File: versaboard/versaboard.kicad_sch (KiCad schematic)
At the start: 23 parts, among them J1 UART, J39 Conn_02x20_Odd_Even, J4 DBG, J40 Conn_02x20_Odd_Even, SW1 RST, U1 ATSAML21G18B-AUT, Y1 32.768kHz

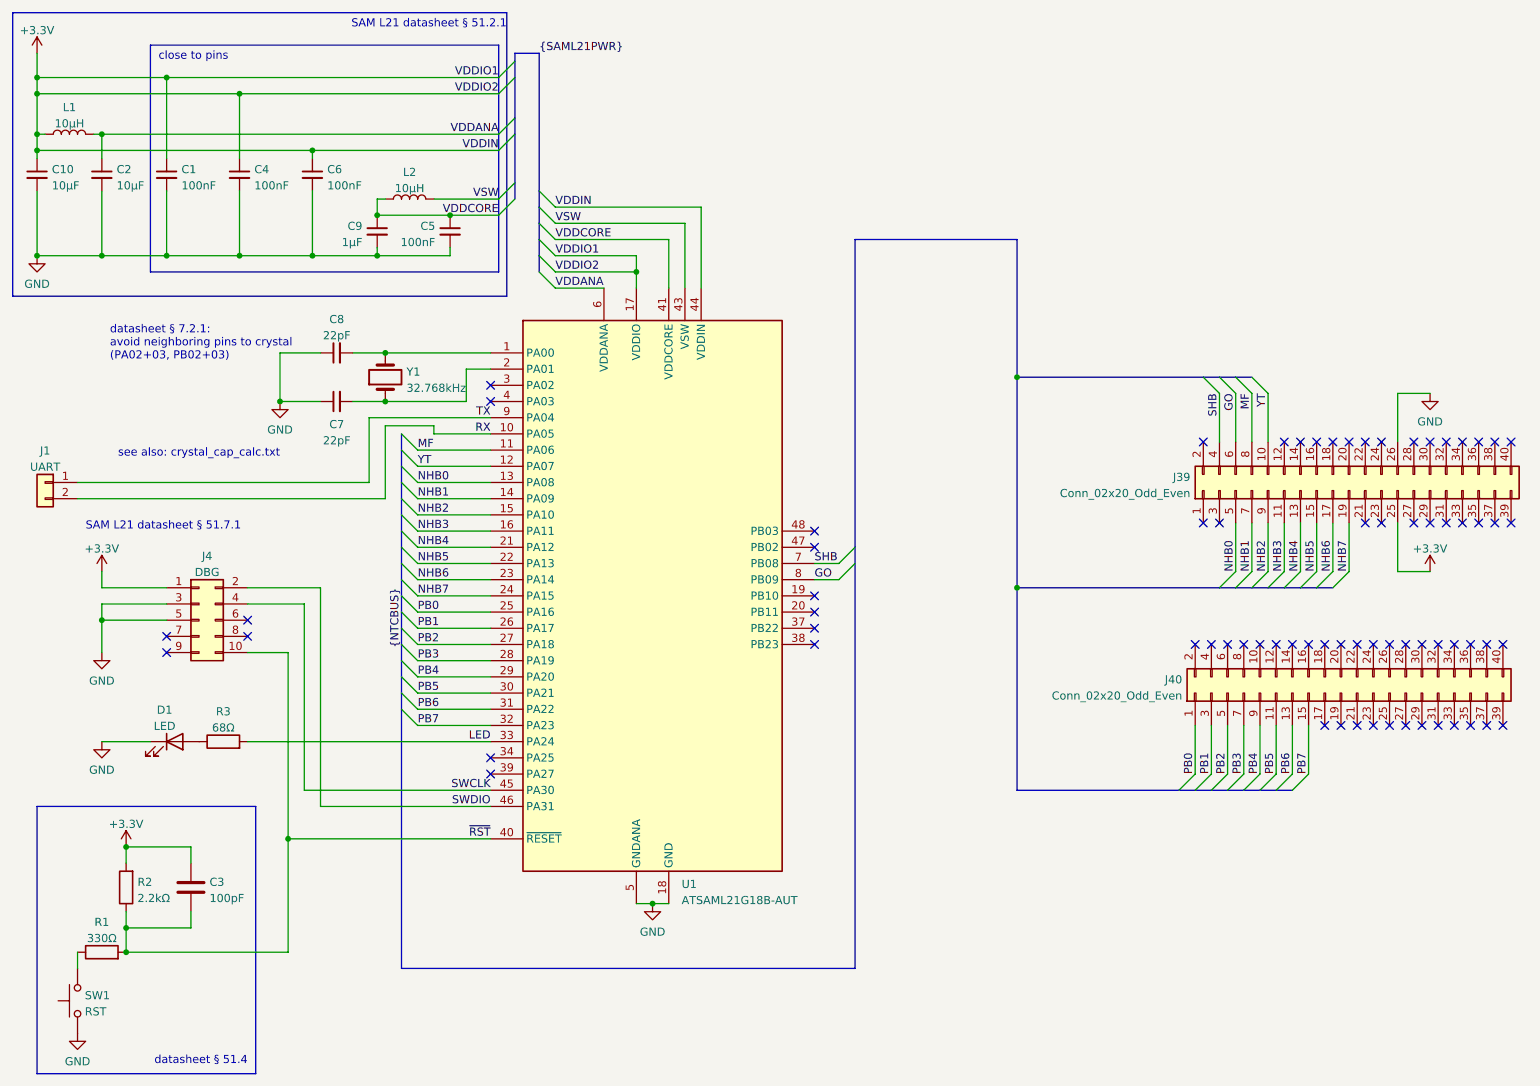
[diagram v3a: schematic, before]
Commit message: versaboard r0002: replace crystal with oscillator, add test points
the crystal on the test run of r0001 does not stabilize; switch to an
oscillator which should manage this without our support

also add a few test points on the board
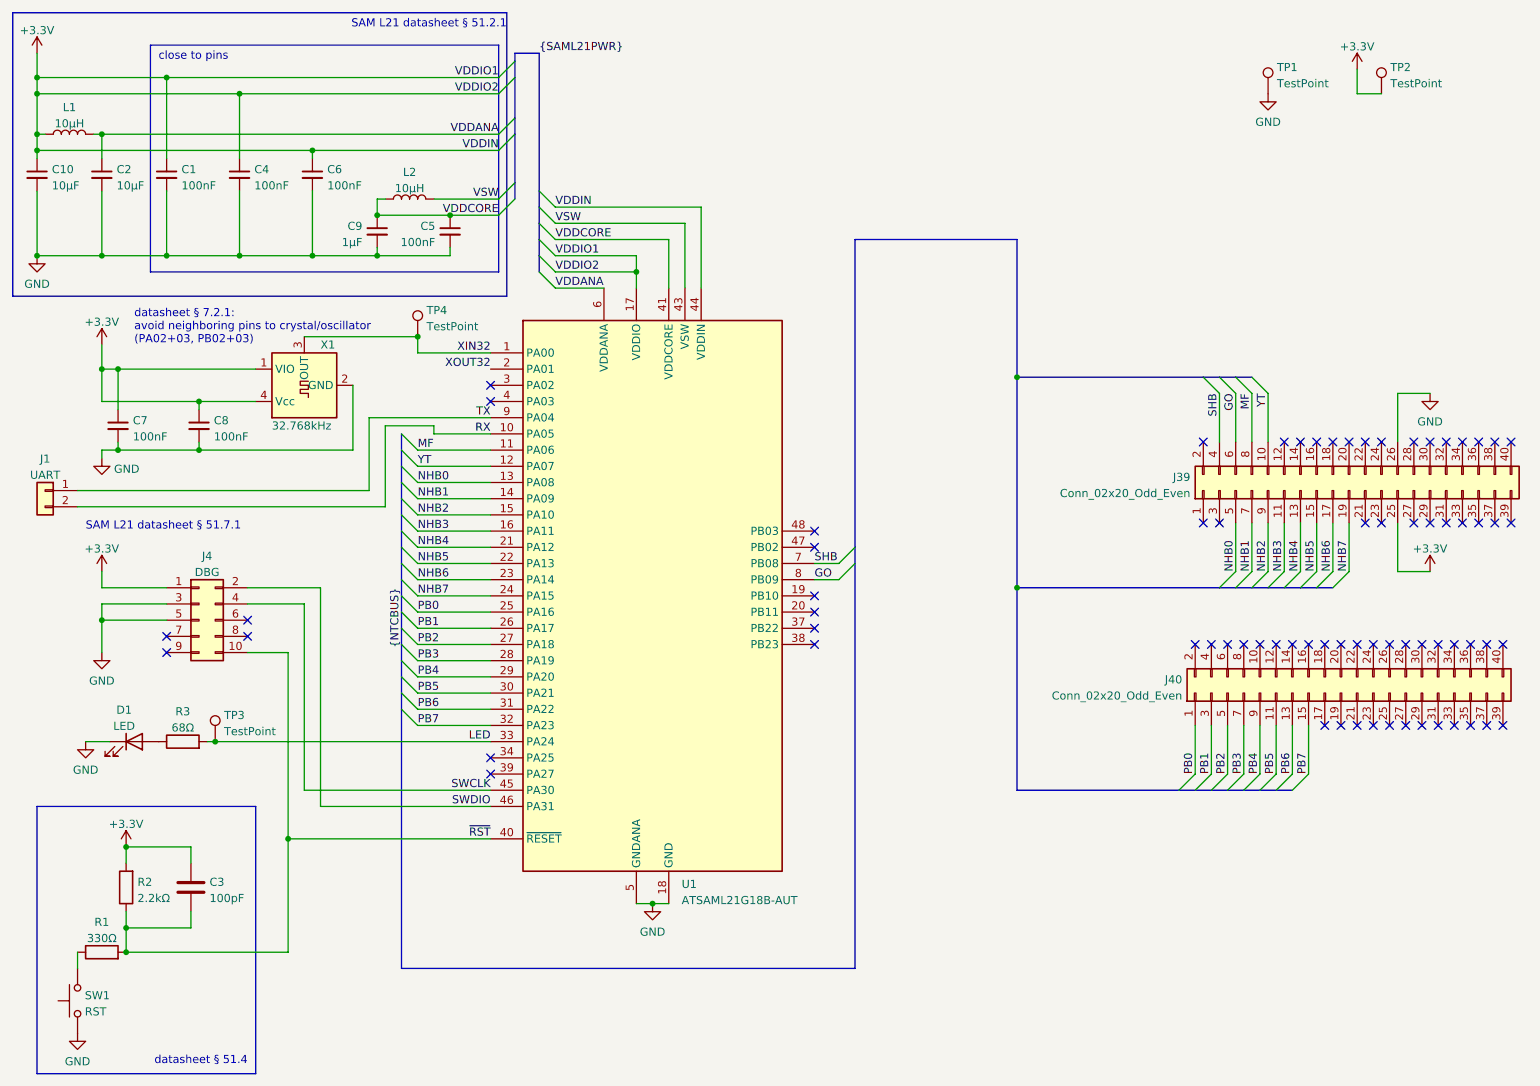
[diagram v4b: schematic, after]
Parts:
- added TP1, TP2, TP3, TP4: TestPoint, TestPoint:TestPoint_Pad_D1.0mm, symbol Connector:TestPoint
- C7, C8: value 22pF -> 100nF; JLCPCB C1555 -> C307331; LCSC C1555 -> C307331
- X1: renamed from Y1; footprint Crystal:Crystal_SMD_3215-2Pin_3.2x1.5mm -> Oscillator:Oscillator_SMD_SeikoEpson_SG3030CM; symbol Device:Crystal -> Oscillator:SG-3030CM; JLCPCB C32346 -> C2976104; LCSC C32346 -> C2976104; Manufacturer (none) -> Seiko Epson; Model (none) -> SG-3031CM
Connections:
- net +3.3V: now also C7.1, C8.1, X1.1 (VIO), X1.4 (Vcc), TP2.1
- net GND: now also C7.2, C8.2, X1.2 (GND), TP1.1; no longer C7.1, C8.1
- net LED: now also TP3.1
- new net XIN32: TP4.1, U1.1 (PA00), X1.3 (OUT)
- new net XOUT32: U1.2 (PA01)
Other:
- note added: "datasheet § 7.2.1: avoid neighboring pins to crystal/oscillator (PA02+03, PB02+03)"
- note removed: "datasheet § 7.2.1: avoid neighboring pins to crystal (PA02+03, PB02+03)"
- note removed: "see also: crystal_cap_calc.txt"
- moved on the sheet: D1, J1, R3

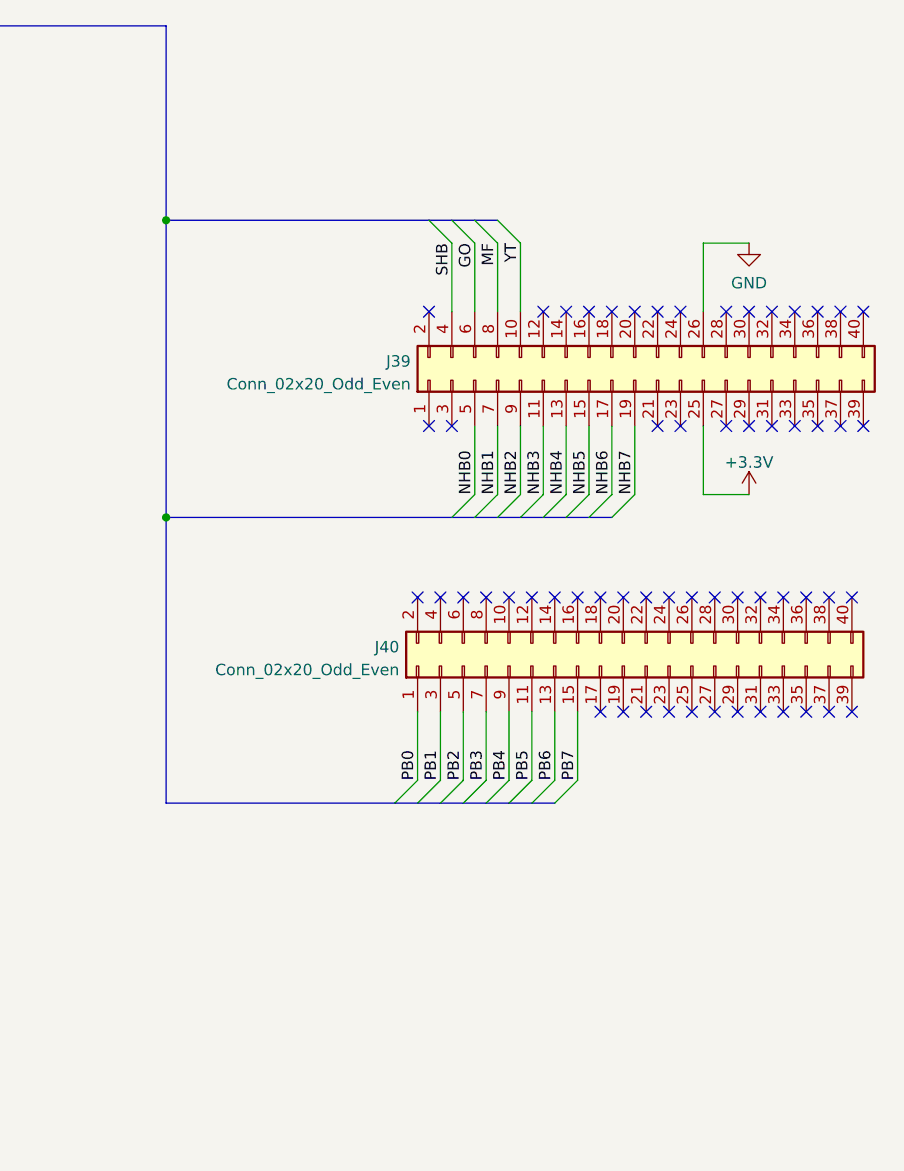
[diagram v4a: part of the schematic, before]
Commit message: versaboard r0003: avoid FPGA pin bank 1
Pin bank 1 on the ECP5 evaluation board is +2.5V by default and this can
only be changed by resoldering SMD resistors. Yeah, no.
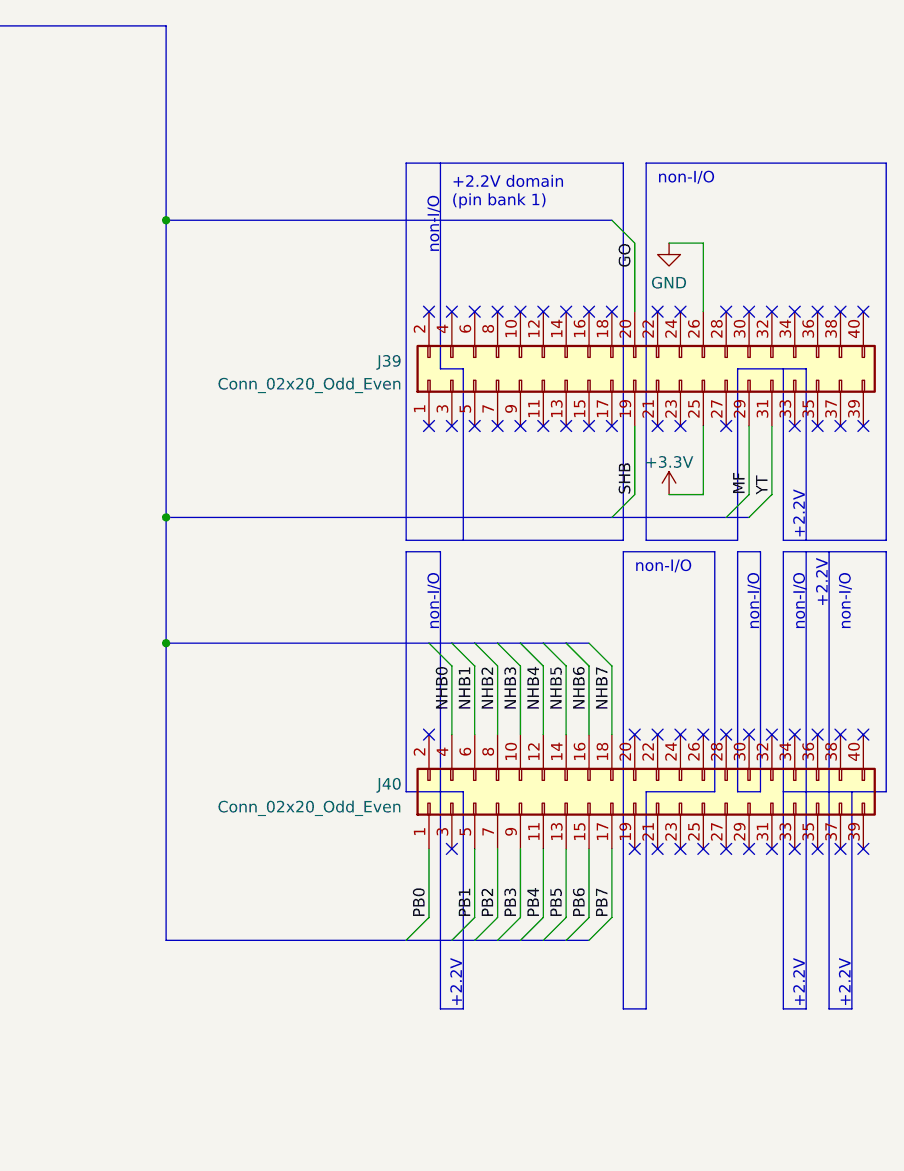
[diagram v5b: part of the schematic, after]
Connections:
- net GO: now also J39.20 (Pin_20); no longer J39.6 (Pin_6)
- net MF: now also J39.29 (Pin_29); no longer J39.8 (Pin_8)
- net NHB0: now also J40.4 (Pin_4); no longer J39.5 (Pin_5)
- net NHB1: now also J40.6 (Pin_6); no longer J39.7 (Pin_7)
- net NHB2: now also J40.8 (Pin_8); no longer J39.9 (Pin_9)
- net NHB3: now also J40.10 (Pin_10); no longer J39.11 (Pin_11)
- net NHB4: now also J40.12 (Pin_12); no longer J39.13 (Pin_13)
- net NHB5: now also J40.14 (Pin_14); no longer J39.15 (Pin_15)
- net NHB6: now also J40.16 (Pin_16); no longer J39.17 (Pin_17)
- net NHB7: now also J40.18 (Pin_18); no longer J39.19 (Pin_19)
- net PB1: now also J40.5 (Pin_5); no longer J40.3 (Pin_3)
- net PB2: now also J40.7 (Pin_7); no longer J40.5 (Pin_5)
- net PB3: now also J40.9 (Pin_9); no longer J40.7 (Pin_7)
- net PB4: now also J40.11 (Pin_11); no longer J40.9 (Pin_9)
- net PB5: now also J40.13 (Pin_13); no longer J40.11 (Pin_11)
- net PB6: now also J40.15 (Pin_15); no longer J40.13 (Pin_13)
- net PB7: now also J40.17 (Pin_17); no longer J40.15 (Pin_15)
- net SHB: now also J39.19 (Pin_19); no longer J39.4 (Pin_4)
- net YT: now also J39.31 (Pin_31); no longer J39.10 (Pin_10)
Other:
- note added: "+2.2V"
- note added: "+2.2V domain (pin bank 1)"
- note added: "non-I/O"
- moved on the sheet: J40

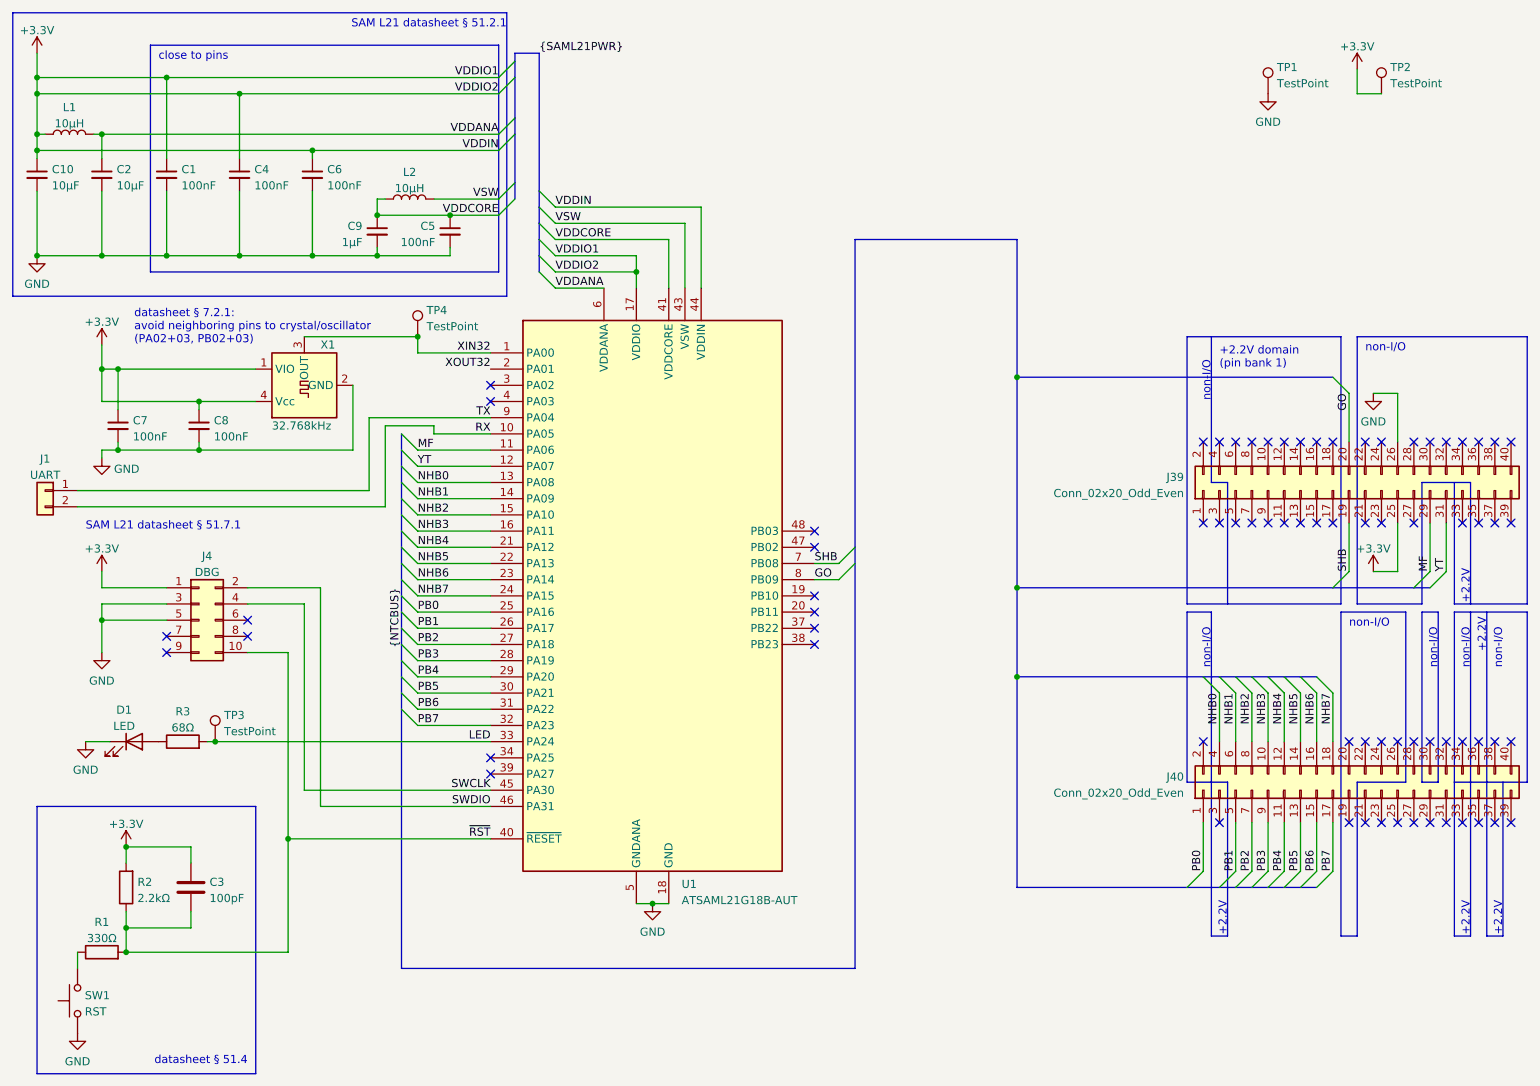
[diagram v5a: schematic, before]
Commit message: versaboard: add STA, STC and SG pins
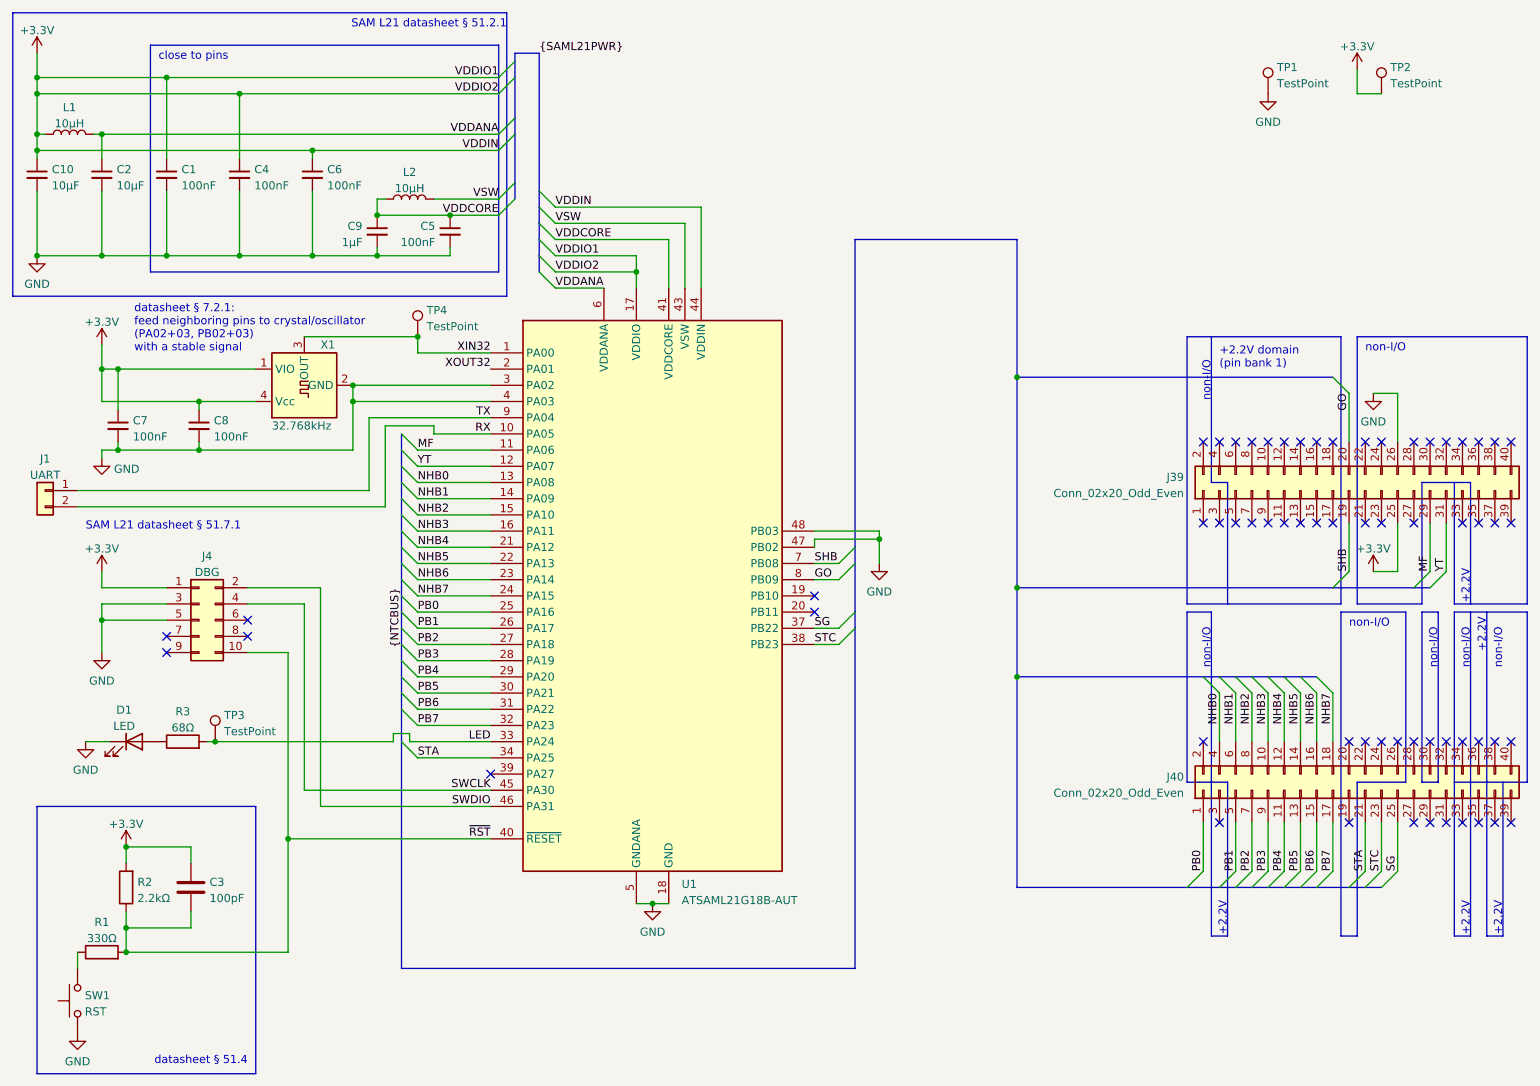
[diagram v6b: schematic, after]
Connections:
- net GND: now also U1.3 (PA02), U1.4 (PA03), U1.47 (PB02), U1.48 (PB03)
- net STA: now reaches U1.34 (PA25)
- net STA: now also J40.21 (Pin_21)
- net SG: now reaches U1.37 (PB22)
- net SG: now also J40.25 (Pin_25)
- net STC: now reaches U1.38 (PB23)
- net STC: now also J40.23 (Pin_23)
- no-connect marks 72 -> 62
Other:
- note added: "datasheet § 7.2.1: feed neighboring pins to crystal/oscillator (PA02+03, PB02+03) with a stable signal"
- note removed: "datasheet § 7.2.1: avoid neighboring pins to crystal/oscillator (PA02+03, PB02+03)"
